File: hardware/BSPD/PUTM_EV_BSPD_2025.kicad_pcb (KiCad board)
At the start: 4 copper layers, 63 x 37.5 mm, 89 parts, among them J1 BS1, J2 BS2, J3 BS2, J4 Conn_01x02, J5 SDC, K2 TE AXICOM IM07DTS, Q1 BS170F, U1 MC78M12CDTG, U10 LM393B, U12 74AHC1G08, U13 LM393B, U2 LM1117IMP-5.0, U3 74HC2G14-Q100, U4 LM393B, U5 74AHC1G08, U6 74HC2G14-Q100, U7 LM393B, U8 NE555DR, U9 74HC1G32GV

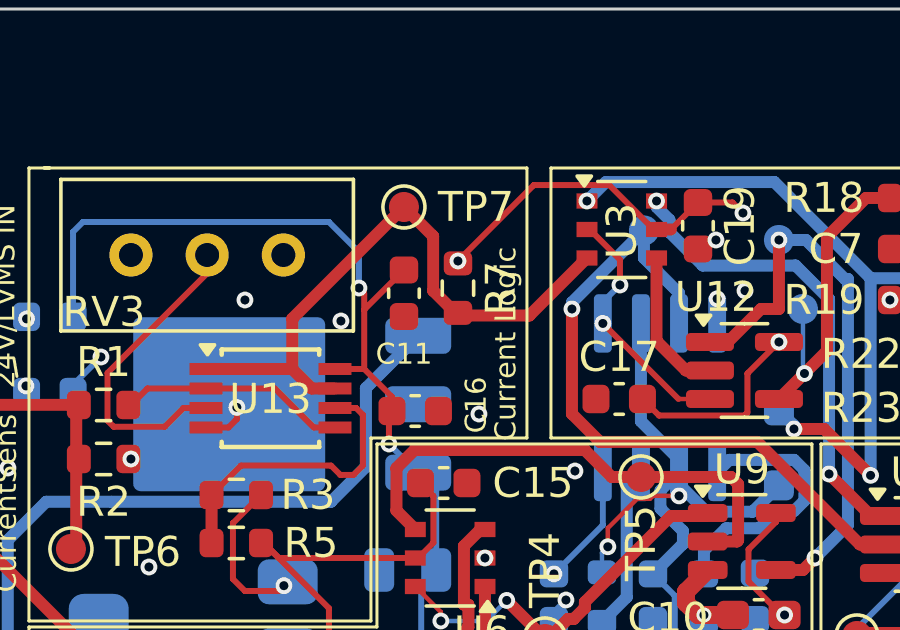
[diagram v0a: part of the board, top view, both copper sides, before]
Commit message: Fixed more silkscreen overlaps
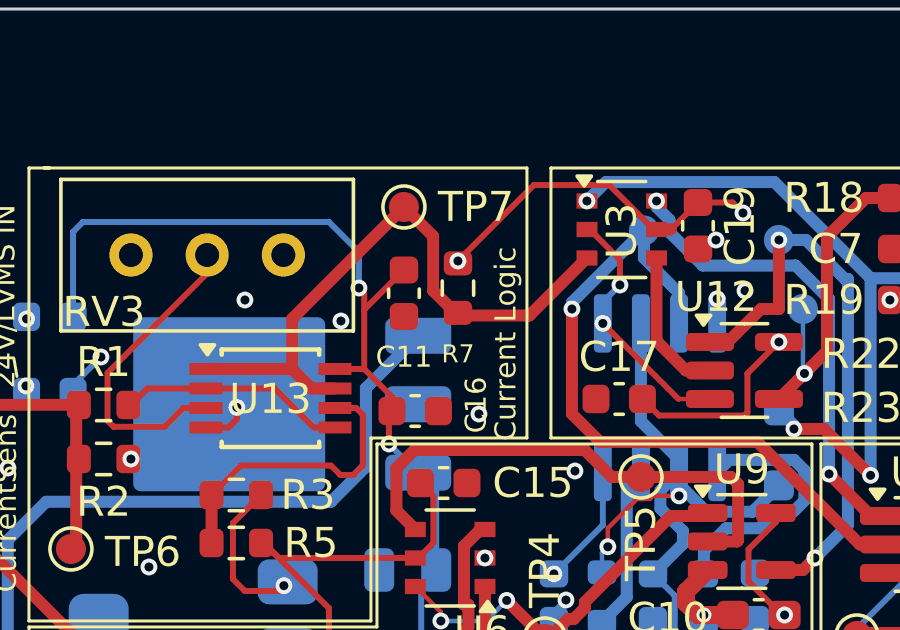
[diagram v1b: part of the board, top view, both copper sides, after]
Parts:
- renumbered 500mA/30V1 to F1
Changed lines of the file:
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@@
 		)
 		(pad_to_mask_clearance 0.038)
-		(solder_mask_min_width 0.08)
 		(allow_soldermask_bridges_in_footprints yes)
 		(tenting front back)
@@
 		(tags "capacitor")
 		(property "Reference" "C11"
-			(at -2.025 0 0)
+			(at -2.125 0 180)
 			(layer "F.SilkS")
 			(effects
@@
 		(tags "resistor")
 		(property "Reference" "R7"
-			(at 0 -1.43 270)
+			(at 2.195 0 0)
 			(layer "F.SilkS")
 			(effects
 				(font
-					(size 1 1)
+					(size 0.6 0.6)
 					(thickness 0.15)
 				)
@@
 		(descr "Diode SMD 1812 (4532 Metric), square (rectangular) end terminal, IPC-7351 nominal, (Body size source: https://www.nikhef.nl/pub/departments/mt/projects/detectorR_D/dtddice/ERJ2G.pdf), generated with kicad-footprint-generator")
 		(tags "diode handsolder")
-		(property "Reference" "500mA/30V1"
-			(at 0 2.65 180)
+		(property "Reference" "F1"
+			(at -4.075 0 180)
 			(layer "B.SilkS")
 			(effects
@@
 		(tags "capacitor")
 		(property "Reference" "C18"
-			(at -3.125 0 90)
+			(at -2.625 0 90)
 			(layer "B.SilkS")
 			(effects
 				(font
-					(size 1 1)
+					(size 0.6 0.6)
 					(thickness 0.15)
 				)

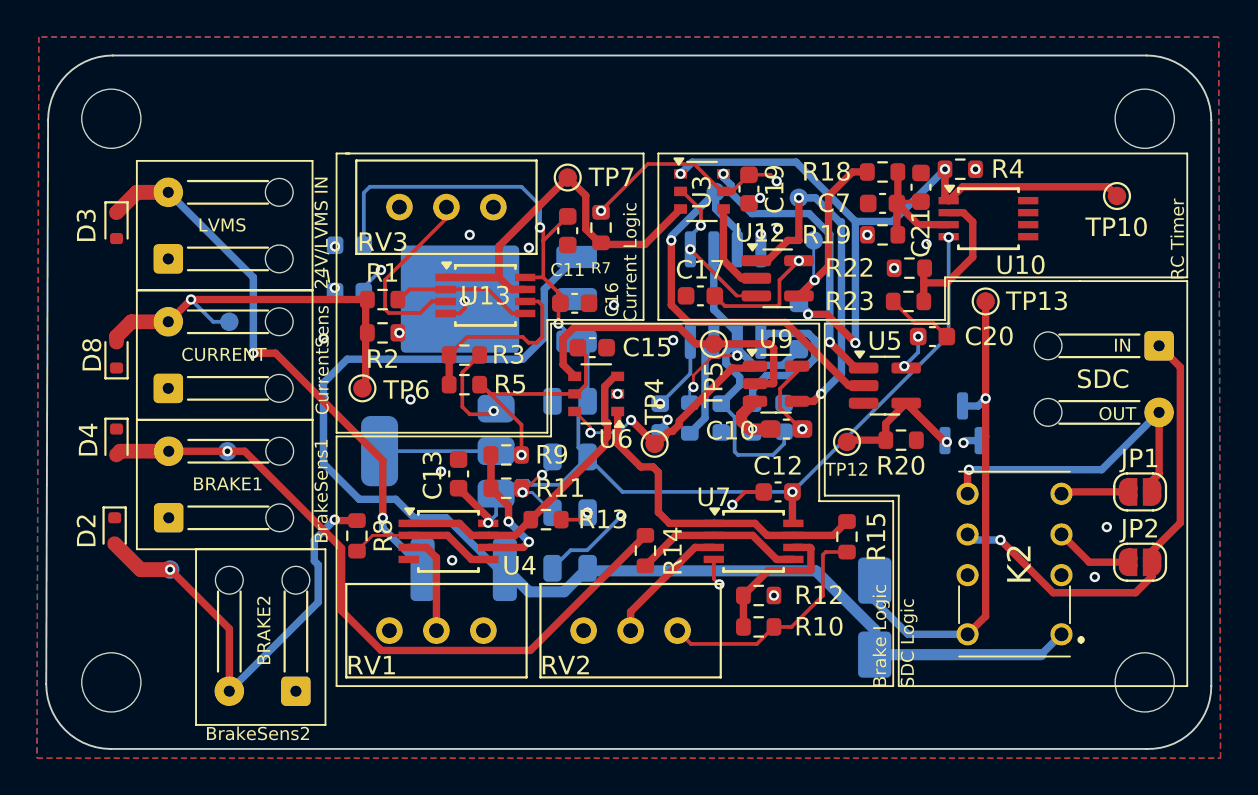
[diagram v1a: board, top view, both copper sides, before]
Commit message: Added silkscreen descriptions
Added descriptions of potentiometers (RV1-RV3) to ease up threshold regulation.
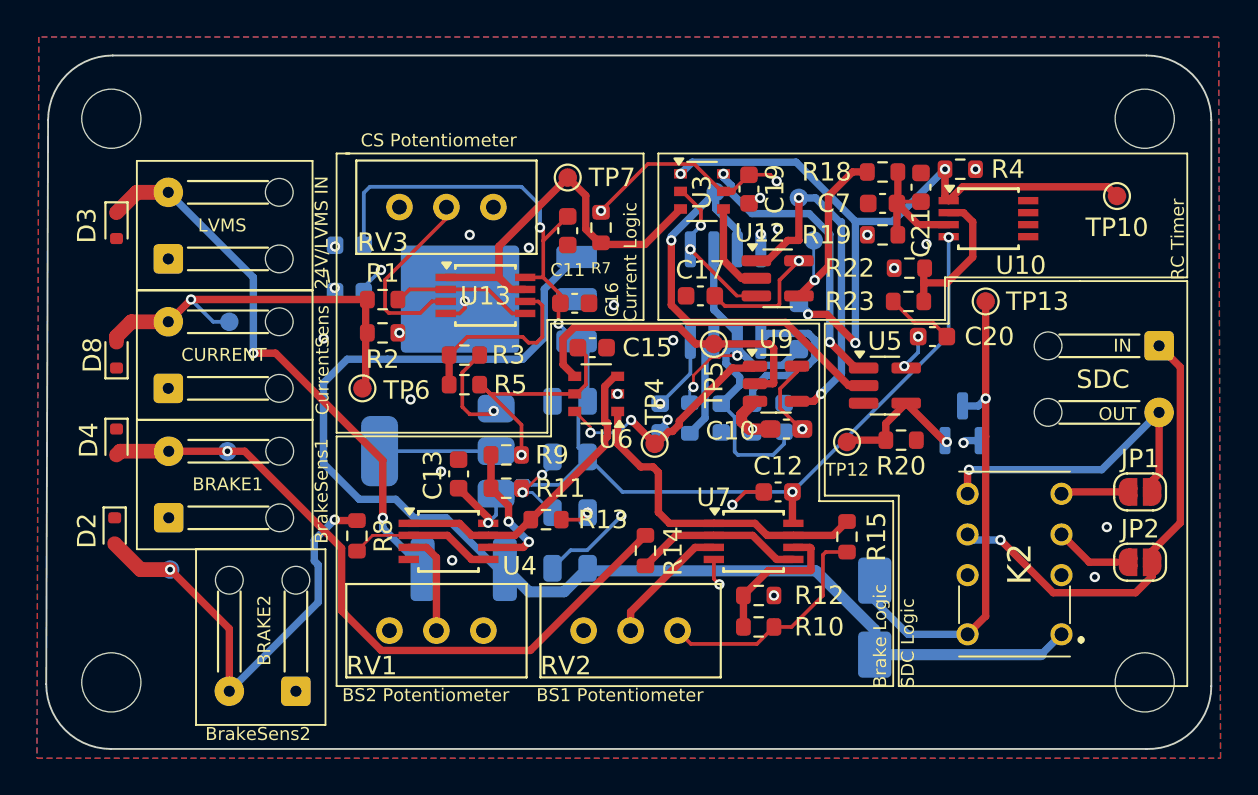
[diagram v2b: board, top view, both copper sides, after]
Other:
- board text added: "BS1 Potentiometer"
- board text added: "BS2 Potentiometer"
- board text added: "CS Potentiometer"
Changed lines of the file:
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@@
 			(psa4output no)
 			(plot_black_and_white yes)
+			(plotinvisibletext no)
 			(sketchpadsonfab no)
 			(plotpadnumbers no)
@@
 		)
 	)
+	(gr_text "BS2 Potentiometer"
+		(at 125.5 119 0)
+		(layer "F.SilkS")
+		(effects
+			(font
+				(size 0.7 0.7)
+				(thickness 0.1)
+			)
+			(justify left bottom)
+		)
+	)
 	(gr_text "BrakeSens1"
 		(at 124.8 110.4 90)
@@
 		)
 	)
+	(gr_text "CS Potentiometer"
+		(at 126.5 89 0)
+		(layer "F.SilkS")
+		(effects
+			(font
+				(size 0.7 0.7)
+				(thickness 0.1)
+			)
+			(justify left bottom)
+		)
+	)
 	(gr_text "BRAKE2"
 		(at 121.7 117 90)
 		(layer "F.SilkS")
 		(effects
+			(font
+				(size 0.7 0.7)
+				(thickness 0.1)
+			)
+			(justify left bottom)
+		)
+	)
+	(gr_text "BS1 Potentiometer"
+		(at 136 119 0)
+		(layer "F.SilkS")
+		(effects

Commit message: Fixed relay control MOSFET pins.
Fixed an issue where the pins of Q1 MOSFET were mismatched comparing to datasheets of picked MOS.
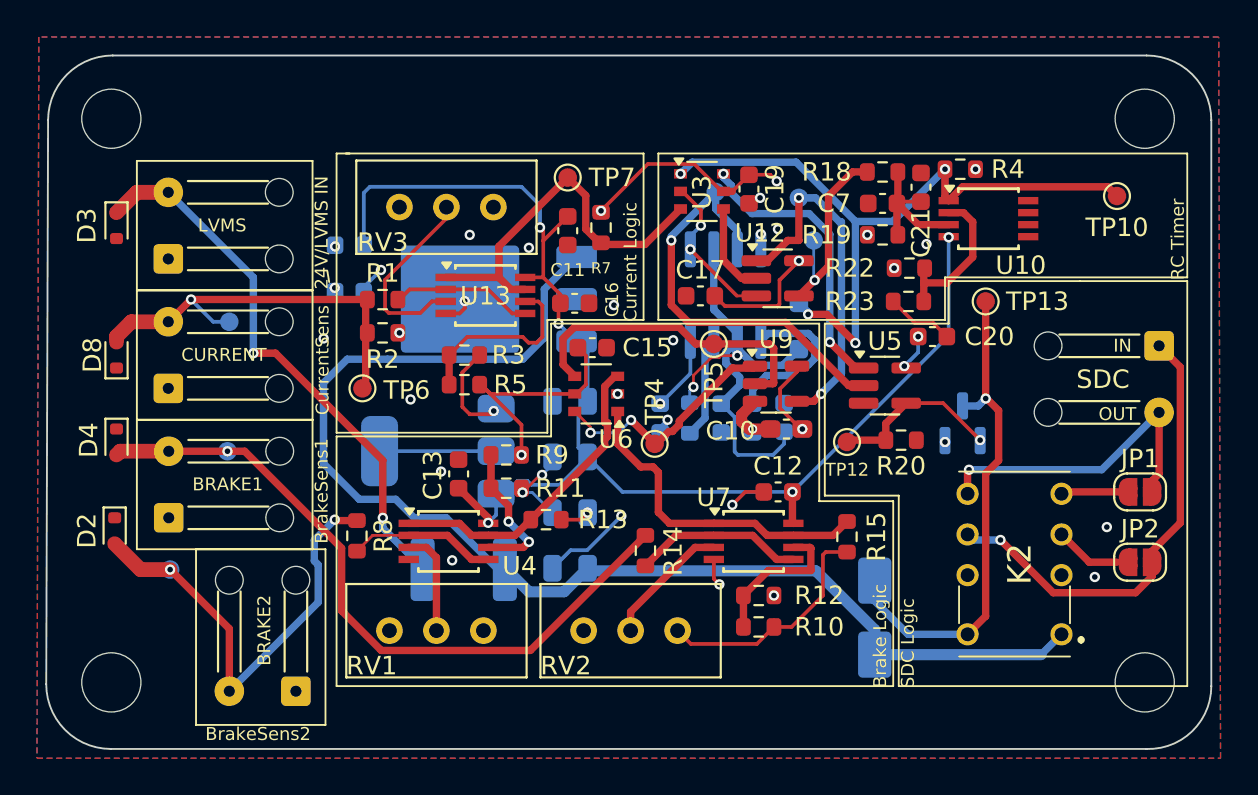
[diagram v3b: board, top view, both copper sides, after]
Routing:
- net Net-(Q1-G): track 7.77 -> 9.43 mm
- net GND: track 42.3 -> 41.5 mm
- net Net-(D1-A): track 26.7 -> 27.3 mm
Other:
- board text removed: "BS1 Potentiometer"
- board text removed: "BS2 Potentiometer"
- board text removed: "CS Potentiometer"
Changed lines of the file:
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@@
 			(psa4output no)
 			(plot_black_and_white yes)
-			(plotinvisibletext no)
 			(sketchpadsonfab no)
 			(plotpadnumbers no)
@@
 		)
 		(pad "2" smd roundrect
-			(at -0.9375 -0.95 90)
+			(at -0.9375 0.95 90)
 			(size 1.475 0.6)
 			(layers "B.Cu" "B.Mask" "B.Paste")
 			(roundrect_rratio 0.25)
 			(net 20 "Net-(Q1-G)")
-			(pinfunction "G")
-			(pintype "input")
+			(pinfunction "S")
+			(pintype "passive")
 		)
 		(pad "3" smd roundrect
-			(at -0.9375 0.95 90)
+			(at -0.9375 -0.95 90)
 			(size 1.475 0.6)
 			(layers "B.Cu" "B.Mask" "B.Paste")
 			(roundrect_rratio 0.25)
 			(net 4 "GND")
-			(pinfunction "S")
-			(pintype "passive")
+			(pinfunction "G")
+			(pintype "input")
 		)
 		(embedded_fonts no)
@@
 		)
 	)
-	(gr_text "BS2 Potentiometer"
-		(at 125.5 119 0)
-		(layer "F.SilkS")
-		(effects
-			(font
-				(size 0.7 0.7)
-				(thickness 0.1)
-			)
-			(justify left bottom)
-		)
-	)
 	(gr_text "BrakeSens1"
 		(at 124.8 110.4 90)
@@
 		)
 	)
-	(gr_text "CS Potentiometer"
-		(at 126.5 89 0)
-		(layer "F.SilkS")
-		(effects
-			(font
-				(size 0.7 0.7)
-				(thickness 0.1)
-			)
-			(justify left bottom)
-		)
-	)
 	(gr_text "BRAKE2"
 		(at 121.7 117 90)
@@
 		)
 	)
-	(gr_text "BS1 Potentiometer"
-		(at 136 119 0)
-		(layer "F.SilkS")
-		(effects
-			(font
-				(size 0.7 0.7)
-				(thickness 0.1)
-			)
-			(justify left bottom)
-		)
-	)
 	(gr_text "RC Timer"
 		(at 171.1 96.15 90)
@@
 	)
 	(via
-		(at 159.1 104.95)
+		(at 158.1 104.9)
 		(size 0.56)
 		(drill 0.3)
@@
 	)
 	(segment
+		(start 158.1 104.9)
+		(end 158.2 104.9)
+		(width 0.4)
+		(layer "B.Cu")
+		(net 4)
+	)
+	(segment
 		(start 136.875 108.72)
 		(end 135.785 107.63)
@@
 	)
 	(segment
-		(start 160 104.825)
-		(end 159.225 104.825)
-		(width 0.4)
-		(layer "B.Cu")
-		(net 4)
-	)
-	(segment
 		(start 142.7 104.380954)
 		(end 142.719046 104.380954)
@@
 	)
 	(segment
-		(start 159.225 104.825)
-		(end 159.1 104.95)
-		(width 0.4)
-		(layer "B.Cu")
-		(net 4)
-	)
-	(segment
 		(start 135.785 107.63)
 		(end 135.255 107.63)
@@
 	)
 	(segment
-		(start 160.3 104.6)
-		(end 160.3 114.32)
+		(start 161 105.9)
+		(end 160.3 106.6)
 		(width 0.4)
 		(layer "F.Cu")
@@
 	)
 	(segment
-		(start 160.3 102.55)
-		(end 160.3 104.6)
+		(start 160.3 114.32)
+		(end 159.32 115.3)
 		(width 0.4)
 		(layer "F.Cu")
@@
 	)
 	(segment
-		(start 160.3 114.32)
-		(end 159.32 115.3)
+		(start 161 103.2)
+		(end 161 105.9)
+		(width 0.4)
+		(layer "F.Cu")
+		(net 9)
+	)
+	(segment
+		(start 160.3 106.6)
+		(end 160.3 114.32)
+		(width 0.4)
+		(layer "F.Cu")
+		(net 9)
+	)
+	(segment
+		(start 160.35 102.55)
+		(end 161 103.2)
+		(width 0.4)
+		(layer "F.Cu")
+		(net 9)
+	)
+	(segment
+		(start 160.3 102.55)
+		(end 160.35 102.55)
 		(width 0.4)
 		(layer "F.Cu")
@@
 	)
 	(segment
-		(start 158.1 104.9)
-		(end 156 102.8)
-		(width 0.4)
+		(start 158 102.8)
+		(end 160 104.8)
+		(width 0.2)
 		(layer "F.Cu")
 		(net 20)
@@
 	)
 	(segment
-		(start 158.2 104.9)
-		(end 158.1 104.9)
+		(start 152.9 104.8)
+		(end 152.8 104.9)
 		(width 0.4)
 		(layer "F.Cu")
@@
 	)
 	(segment
-		(start 152.9 104.8)
-		(end 152.8 104.9)
-		(width 0.4)
+		(start 156 102.8)
+		(end 158 102.8)
+		(width 0.2)
 		(layer "F.Cu")
 		(net 20)
@@
 	)
 	(via
-		(at 158.2 104.9)
+		(at 160 104.8)
 		(size 0.56)
 		(drill 0.3)
@@
 		(net 20)
 	)
-	(segment
-		(start 158.1 104.9)
-		(end 158.2 104.9)
-		(width 0.4)
-		(layer "B.Cu")
-		(net 20)
-	)

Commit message: Changes for 2026 Rules - added pull down resistors and reversed polarity of comparator (nie pozdrawiam Zdrajcy)
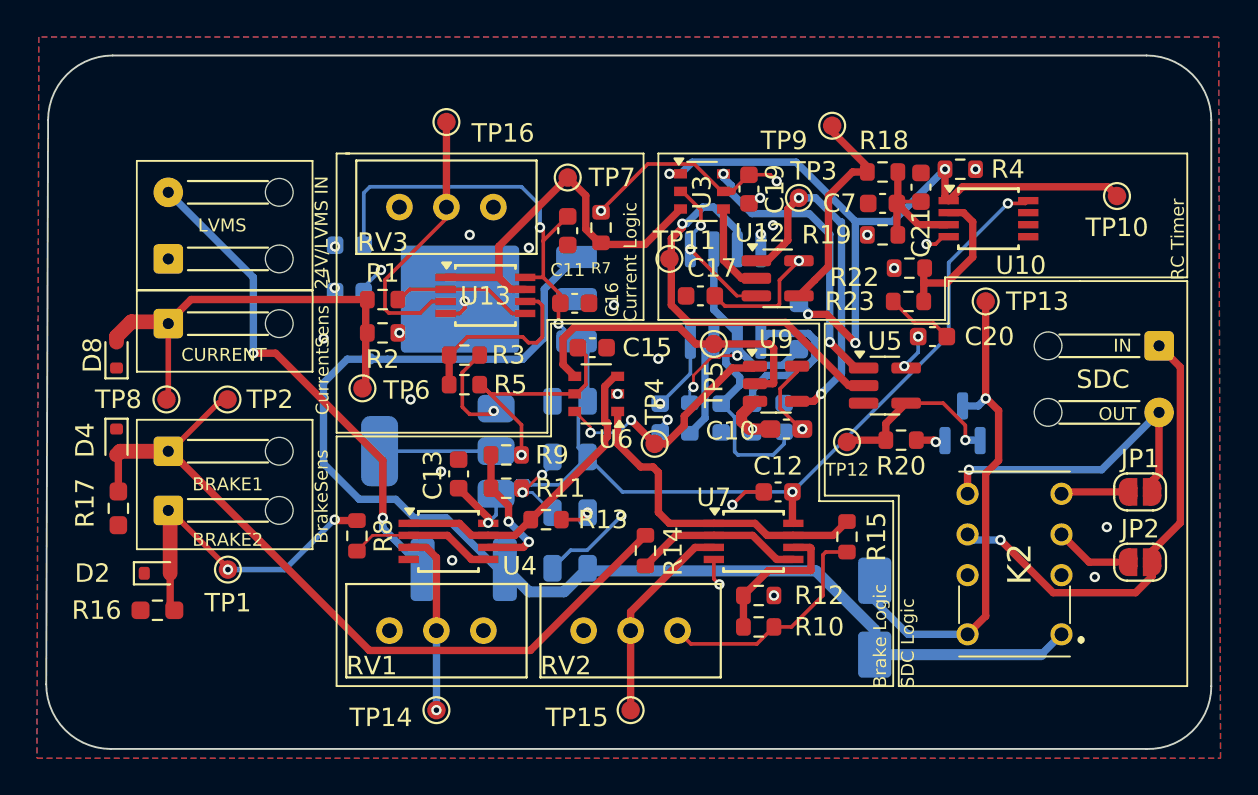
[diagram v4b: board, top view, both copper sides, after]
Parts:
- removed H1, H2, H3, H4: MountingHole, MountingHole:MountingHole_3.2mm_M3_ISO7380
- added R16: 100K, Resistor_SMD:R_0603_1608Metric_Pad0.98x0.95mm_HandSolder, F.Cu at (115.5, 114.0)
- added R17: 100K, Resistor_SMD:R_0603_1608Metric_Pad0.98x0.95mm_HandSolder, F.Cu at (113.4, 108.5)
- added TP14: TestPoint, TestPoint:TestPoint_Pad_D1.0mm, F.Cu at (130.6, 119.4)
- added TP15: TestPoint, TestPoint:TestPoint_Pad_D1.0mm, F.Cu at (141.1, 119.4)
- added TP16: TestPoint, TestPoint:TestPoint_Pad_D1.0mm, F.Cu at (131.1, 87.6)
- D3: moved to B.Cu
- J1: footprint footprints:Wire_StrainRelief -> Connector_Wire:SolderWire-0.1sqmm_1x01_D0.4mm_OD1mm_Relief
- J2, J3: value BS2 -> BS1; footprint footprints:Wire_StrainRelief -> Connector_Wire:SolderWire-0.1sqmm_1x01_D0.4mm_OD1mm_Relief
- TP1, TP11, TP2, TP3, TP8, TP9: moved to F.Cu
- moved D3 15.1 mm to (126.9, 99.7), turned to 90 degrees
- moved J1 8.36 mm to (116.1, 108.6), turned to 90 degrees
- moved TP9 6.28 mm to (152.0, 87.8), turned to 180 degrees
- moved TP8 5.40 mm to (116.0, 102.6), turned to 180 degrees
- moved TP11 4.40 mm to (143.2, 95.0)
- moved J2 3.65 mm to (116.1, 105.4)
- moved J3 3.58 mm to (116.1, 98.5)
- moved D2 3.25 mm to (115.5, 112.0), turned to 0 degrees
- moved TP1 3.12 mm to (119.3, 111.8), turned to 180 degrees
- moved TP2 2.80 mm to (119.3, 102.6), turned to 180 degrees
- turned TP3 to 0 degrees
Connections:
- D3 pad 1: Net-(J4-Pin_2) -> /LVMS_Coil
- J1 pad 1: GND -> /Brake Sensors Comparators/Brake2
- J2 pad 1: GND -> /Brake Sensors Comparators/Brake1
- J3 pad 1: GND -> /LEM Comparator/LEM_OpAmp_Out
- U10 pad 4: +12V -> GND
- U10 pad 8: GND -> +12V
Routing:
- net /Brake Sensors Comparators/Brake2: track 24.5 -> 18.2 mm
- net Net-(U13A-+): track 10.5 -> 15.1 mm
- net +12V: track 72.1 -> 76.5 mm
- net Net-(U7A-+): track 6.96 -> 11.3 mm
- net Net-(U4A-+): track 5.68 -> 9.98 mm, vias 0 -> 1
- net /Brake Sensors Comparators/Brake1: track 37.7 -> 41.9 mm, vias 1 -> 0
- net Net-(J4-Pin_2): track 29.7 -> 26.5 mm
- net GND: track 41.5 -> 44.4 mm
- net Net-(D5-A): track 39.1 -> 40.3 mm
- net Net-(U8-Q): track 22.9 -> 21.7 mm
- net /LEM Comparator/LEM_OpAmp_Out: track 22.2 -> 23.3 mm, vias 1 -> 0
- net Net-(R18-Pad1): track 10.9 -> 12.0 mm, vias 1 -> 0
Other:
- board text added: "BrakeSens"
- board text removed: "BrakeSens1"
- board text removed: "BrakeSens2"
